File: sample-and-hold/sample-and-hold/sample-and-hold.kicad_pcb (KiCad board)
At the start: 2 copper layers, 36 parts, among them J1 Power Connector, J2 CLOCK_IN, J3 SIGNAL_IN, J4 SIGNAL_IN, Q1 J112, Q2 2N3904, U1 TL072, U2 TL072

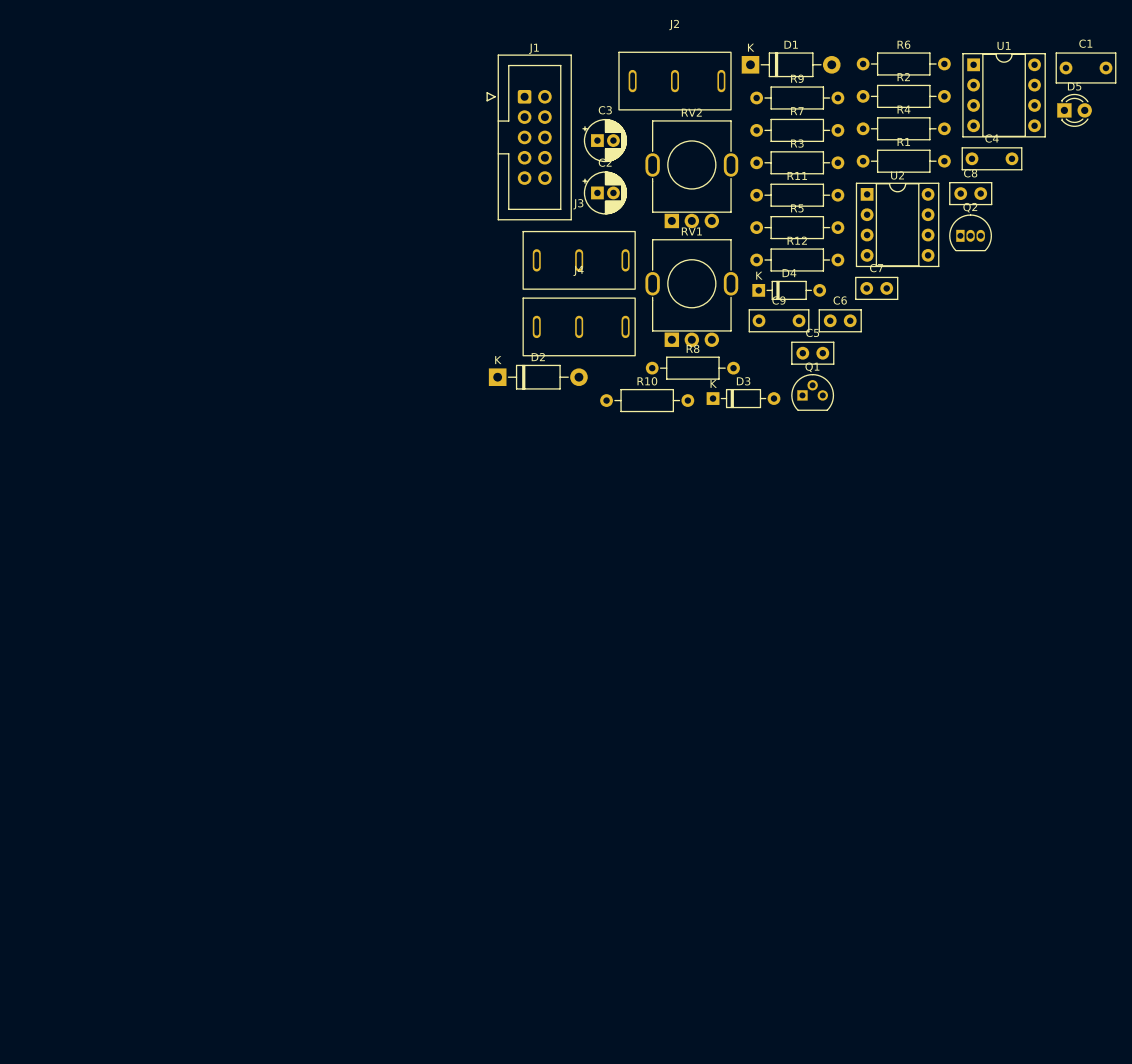
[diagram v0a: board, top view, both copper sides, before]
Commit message: Added REV1 of sample and hold board/panel
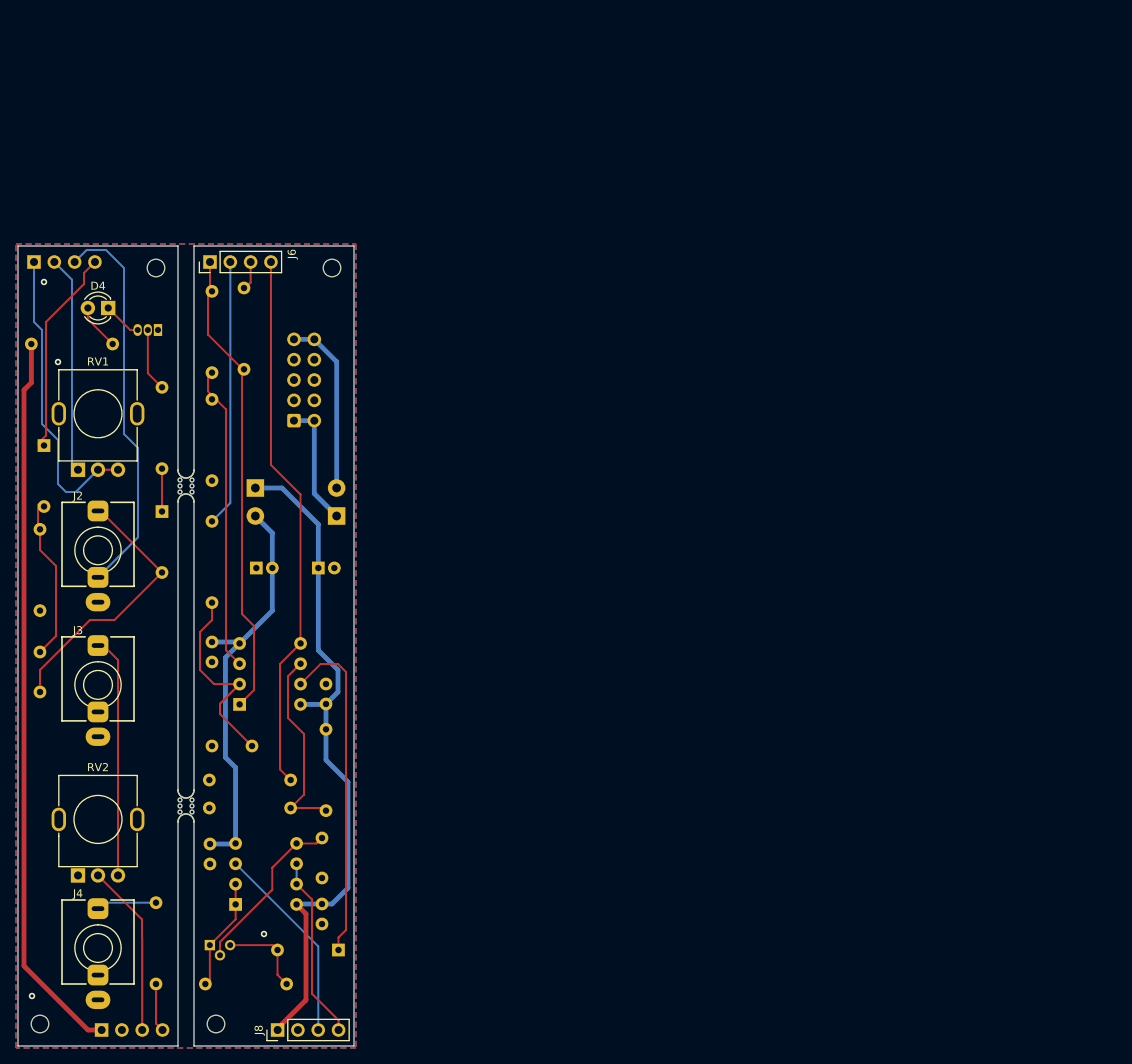
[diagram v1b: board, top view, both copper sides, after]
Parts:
- added D6: 1N4148, Diode_THT:D_DO-35_SOD27_P7.62mm_Horizontal, B.Cu at (180.1, 132.2)
- added H1: MountingHole, MountingHole:MountingHole_2.2mm_M2, F.Cu at (157.2, 47.0)
- added H2: MountingHole, MountingHole:MountingHole_2.2mm_M2, F.Cu at (142.8, 141.5)
- added H3: MountingHole, MountingHole:MountingHole_2.2mm_M2, F.Cu at (179.2, 47.0)
- added H4: MountingHole, MountingHole:MountingHole_2.2mm_M2, F.Cu at (164.8, 141.5)
- added J6: BACK_TOP, Connector_PinHeader_2.54mm:PinHeader_1x04_P2.54mm_Vertical, F.Cu at (164.0, 46.2)
- added J7: FRONT_BOTTOM, Connector_PinHeader_2.54mm:PinHeader_1x04_P2.54mm_Vertical, B.Cu at (150.4, 142.2)
- added J8: BACK_BOTTOM, Connector_PinHeader_2.54mm:PinHeader_1x04_P2.54mm_Vertical, F.Cu at (172.4, 142.2)
- added locked: FRONT_TOP, Connector_PinHeader_2.54mm:PinHeader_1x04_P2.54mm_Vertical, B.Cu at (142.0, 46.2)
- added mouse-bite-2mm-slot: VAL**, Panelization:mouse-bite-2mm-slot, F.Cu at (161.0, 74.2)
- added mouse-bite-2mm-slot: VAL**, Panelization:mouse-bite-2mm-slot, F.Cu at (161.0, 114.2)
- C1: value 1uF -> 10uF; footprint Capacitor_THT:C_Rect_L7.2mm_W3.5mm_P5.00mm_FKS2_FKP2_MKS2_MKP2 -> Capacitor_THT:CP_Radial_D5.0mm_P2.00mm; moved to B.Cu
- C2, C5, C6, C7, C9, D1, D2, D3, J1, R4, R5, U1, U2: moved to B.Cu
- C3: value 10uF -> 1nF; footprint Capacitor_THT:CP_Radial_D5.0mm_P2.00mm -> Capacitor_THT:C_Rect_L7.2mm_W2.5mm_P5.00mm_FKS2_FKP2_MKS2_MKP2; moved to B.Cu
- C4: value 1nF -> 0.1uF; footprint Capacitor_THT:C_Rect_L7.2mm_W2.5mm_P5.00mm_FKS2_FKP2_MKS2_MKP2 -> Capacitor_THT:C_Disc_D5.0mm_W2.5mm_P2.50mm; moved to B.Cu
- C8: value 0.1uF -> 1uF; footprint Capacitor_THT:C_Disc_D5.0mm_W2.5mm_P2.50mm -> Capacitor_THT:C_Rect_L7.2mm_W3.5mm_P5.00mm_FKS2_FKP2_MKS2_MKP2; moved to B.Cu
- D4: value 1N4148 -> LED; footprint Diode_THT:D_DO-35_SOD27_P7.62mm_Horizontal -> LED_THT:LED_D3.0mm
- D5: value LED -> 1N4148; footprint LED_THT:LED_D3.0mm -> Diode_THT:D_DO-35_SOD27_P7.62mm_Horizontal; moved to B.Cu
- J2, J3: footprint Tayda_Jacks:PJ-323M -> AudioJacks:Jack_3.5mm_QingPu_WQP-PJ398SM_Vertical
- J4: value SIGNAL_IN -> SIGNAL_OUT; footprint Tayda_Jacks:PJ-323M -> AudioJacks:Jack_3.5mm_QingPu_WQP-PJ398SM_Vertical
- Q1: value J112 -> 2N3904; footprint Package_TO_SOT_THT:TO-92 -> Package_TO_SOT_THT:TO-92_Inline; moved to B.Cu
- Q2: value 2N3904 -> J112; footprint Package_TO_SOT_THT:TO-92_Inline -> Package_TO_SOT_THT:TO-92; moved to B.Cu
- R1, R3: value 100k -> 1k; moved to B.Cu
- R10: value 51k -> 1M; moved to B.Cu
- R11, R12: value 1k -> 100k; moved to B.Cu
- R2: value 2k -> 51k; moved to B.Cu
- R6: value 100k -> 68k; moved to B.Cu
- R7: value 68k -> 100k; moved to B.Cu
- R8: value 100k -> 2k; moved to B.Cu
- R9: value 1M -> 100k; moved to B.Cu
- moved R1 135.6 mm to (157.2, 136.5), turned to 90 degrees
- moved D5 134.3 mm to (143.2, 69.2), turned to -90 degrees
- moved Q2 129.1 mm to (164.0, 131.6)
- moved U1 121.7 mm to (167.7, 101.5)
- moved R4 119.2 mm to (142.8, 89.8), turned to 90 degrees
- moved U2 118.8 mm to (167.2, 126.5)
- moved R6 117.3 mm to (174.1, 114.5), turned to 180 degrees
- moved C8 116.3 mm to (164.2, 106.8)
- moved C4 112.6 mm to (164.2, 93.8), turned to -90 degrees
- moved C1 112.4 mm to (177.5, 84.5)
- moved RV2 110.5 mm to (150.0, 115.9)
- moved C7 102.7 mm to (178.0, 126.5), turned to -90 degrees
- moved C6 101.4 mm to (164.0, 119.0), turned to -90 degrees
- moved J4 98.2 mm to (150.0, 132.0)
- moved C3 98.0 mm to (142.8, 100.0), turned to 90 degrees
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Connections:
- C1 pad 1: GND -> +12V
- C1 pad 2: Net-(C1-Pad2) -> GND
- C2 pad 1: +12V -> GND
- C2 pad 2: GND -> -12V
- C3 pad 1: GND -> Net-(C3-Pad1)
- C3 pad 2: -12V -> Net-(C3-Pad2)
- C4 pad 1: CLK -> -12V
- C4 pad 2: Net-(C4-Pad2) -> GND
- C5 pad 1: -12V -> +12V
- C6 pad 1: +12V -> -12V
- C7 pad 1: -12V -> +12V
- C8 pad 1: +12V -> GND
- C8 pad 2: GND -> Net-(C8-Pad2)
- D3 pad 2: Net-(C4-Pad2) -> Net-(C3-Pad1)
- D5 pad 1: Net-(D5-Pad1) -> /CLK_FRONT
- D5 pad 2: Net-(D5-Pad2) -> Net-(C3-Pad2)
- J2 pad T: CLK -> Net-(C3-Pad1)
- J2 pad TN: INTERNAL_CLK -> /INT_CLK_FRONT
- Q1 pad 1: Net-(Q1-Pad1) -> GND
- Q1 pad 2: Net-(C9-Pad2) -> Net-(Q1-Pad2)
- Q1 pad 3: Net-(D4-Pad2) -> Net-(D4-Pad1)
- Q2 pad 1: GND -> Net-(Q2-Pad1)
- Q2 pad 2: Net-(Q2-Pad2) -> Net-(C9-Pad2)
- Q2 pad 3: Net-(D5-Pad1) -> Net-(D6-Pad2)
- R1 pad 1: Net-(R1-Pad1) -> /OUT_FRONT
- R1 pad 2: GND -> Net-(J4-PadT)
- R10 pad 1: Net-(Q2-Pad2) -> Net-(D6-Pad2)
- R10 pad 2: CLK -> Net-(Q2-Pad1)
- R11 pad 1: +12V -> /RATE_RTN_BACK
- R11 pad 2: Net-(D5-Pad2) -> Net-(R11-Pad2)
- R12 pad 1: Net-(R12-Pad1) -> /INT_CLK_BACK
- R12 pad 2: Net-(J4-PadT) -> /RATE_RTN_BACK
- R2 pad 1: Net-(R2-Pad1) -> Net-(Q1-Pad2)
- R2 pad 2: Net-(C1-Pad2) -> Net-(D3-Pad1)
- R3 pad 1: Net-(R3-Pad1) -> +12V
- R3 pad 2: Net-(R1-Pad1) -> Net-(D4-Pad2)
- R4 pad 1: INTERNAL_CLK -> GND
- R4 pad 2: Net-(R3-Pad1) -> Net-(C3-Pad2)
- R5 pad 2: Net-(C4-Pad2) -> /CLK_BACK
- R6 pad 1: GND -> Net-(R6-Pad1)
- R6 pad 2: Net-(D3-Pad1) -> GND
- R7 pad 1: Net-(R7-Pad1) -> Net-(R11-Pad2)
- R8 pad 1: +12V -> /RATE_SEND_BACK
- R8 pad 2: Net-(R7-Pad1) -> Net-(C8-Pad2)
- R9 pad 1: Net-(D4-Pad2) -> +12V
- R9 pad 2: Net-(Q1-Pad1) -> Net-(R6-Pad1)
- RV1 pad 1: Net-(R2-Pad1) -> /RATE_SEND_FRONT
- RV1 pad 2: Net-(R3-Pad1) -> /RATE_RTN_FRONT
- RV1 pad 3: Net-(R3-Pad1) -> /RATE_RTN_FRONT
- RV2 pad 1: Net-(J3-PadT) -> GND
- RV2 pad 2: Net-(RV2-Pad2) -> /IN_FRONT
- RV2 pad 3: GND -> Net-(J3-PadT)
- U1 pad 1: Net-(R3-Pad1) -> /RATE_RTN_BACK
- U1 pad 2: Net-(C1-Pad2) -> Net-(C8-Pad2)
- U1 pad 3: Net-(R1-Pad1) -> Net-(R11-Pad2)
- U1 pad 5: Net-(D3-Pad1) -> /CLK_BACK
- U1 pad 6: Net-(R7-Pad1) -> Net-(R6-Pad1)
- U1 pad 7: Net-(D4-Pad1) -> Net-(D6-Pad1)
- U2 pad 1: Net-(Q1-Pad1) -> Net-(Q2-Pad1)
- U2 pad 2: Net-(Q1-Pad1) -> Net-(Q2-Pad1)
- U2 pad 3: Net-(RV2-Pad2) -> /IN_BACK
- U2 pad 6: Net-(R12-Pad1) -> /OUT_BACK
- U2 pad 7: Net-(R12-Pad1) -> /OUT_BACK
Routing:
- net +12V: track 0.00 -> 176.9 mm
- net /CLK_BACK: track 0.00 -> 67.9 mm
- net /RATE_RTN_BACK: track 0.00 -> 58.2 mm
- net -12V: track 0.00 -> 51.2 mm
- net /INT_CLK_FRONT: track 0.00 -> 49.2 mm
- net Net-(D6-Pad1): track 0.00 -> 42.3 mm
- net Net-(R11-Pad2): track 0.00 -> 38.4 mm
- net /RATE_RTN_FRONT: track 0.00 -> 38.1 mm
- net Net-(C3-Pad1): track 0.00 -> 33.9 mm
- net /RATE_SEND_BACK: track 0.00 -> 33.4 mm
- net Net-(J3-PadT): track 0.00 -> 29.5 mm
- net /RATE_SEND_FRONT: track 0.00 -> 26.1 mm
- net /CLK_FRONT: track 0.00 -> 25.6 mm
- net Net-(C8-Pad2): track 0.00 -> 25.1 mm
- net /IN_BACK: track 0.00 -> 25.1 mm
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- added copper zone on B.Cu, net GND
- added copper zone on F.Cu, net GND
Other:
- board outline added: 42 x 100 mm

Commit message: Added revision text to sample and hold board/panel
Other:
- board text added: "Northridge Devices - Sept 2022"
- board text added: "S&H Board A - REV1"
- board text added: "S&H Board B - REV1"
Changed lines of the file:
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@@
     (fp_arc (start -2 -1) (mid -1 0) (end -2 1) (layer "F.SilkS") (width 0.1))
     (fp_arc (start 2 1) (mid 1 0) (end 2 -1) (layer "F.SilkS") (width 0.1))
+    (fp_circle (center -2 0) (end -2 -0.06) (layer "Dwgs.User") (width 0.05) (fill none))
     (fp_circle (center 2 0) (end 2.06 0) (layer "Dwgs.User") (width 0.05) (fill none))
-    (fp_circle (center -2 0) (end -2 -0.06) (layer "Dwgs.User") (width 0.05) (fill none))
     (fp_line (start -2 0) (end -2 0) (layer "Eco1.User") (width 2))
     (fp_line (start 2 0) (end 2 0) (layer "Eco1.User") (width 2))
+    (pad "" np_thru_hole circle locked (at 0 -0.75 90) (size 0.5 0.5) (drill 0.5) (layers *.Cu *.Mask))
+    (pad "" np_thru_hole circle locked (at 0.75 -0.75 90) (size 0.5 0.5) (drill 0.5) (layers *.Cu *.Mask))
     (pad "" np_thru_hole circle locked (at 0.75 0.75 90) (size 0.5 0.5) (drill 0.5) (layers *.Cu *.Mask))
+    (pad "" np_thru_hole circle locked (at 0 0.75 90) (size 0.5 0.5) (drill 0.5) (layers *.Cu *.Mask))
+    (pad "" np_thru_hole circle locked (at -0.75 -0.75 90) (size 0.5 0.5) (drill 0.5) (layers *.Cu *.Mask))
     (pad "" np_thru_hole circle locked (at -0.75 0.75 90) (size 0.5 0.5) (drill 0.5) (layers *.Cu *.Mask))
-    (pad "" np_thru_hole circle locked (at -0.75 -0.75 90) (size 0.5 0.5) (drill 0.5) (layers *.Cu *.Mask))
-    (pad "" np_thru_hole circle locked (at 0 0.75 90) (size 0.5 0.5) (drill 0.5) (layers *.Cu *.Mask))
-    (pad "" np_thru_hole circle locked (at 0.75 -0.75 90) (size 0.5 0.5) (drill 0.5) (layers *.Cu *.Mask))
-    (pad "" np_thru_hole circle locked (at 0 -0.75 90) (size 0.5 0.5) (drill 0.5) (layers *.Cu *.Mask))
   )
   (footprint "MountingHole:MountingHole_2.2mm_M2" locked (layer "F.Cu")
@@
   (gr_arc (start 162 112.25) (mid 161 113.25) (end 160 112.25) (layer "Edge.Cuts") (width 0.1))
   (gr_line locked (start 182 44.25) (end 182 144.25) (layer "Edge.Cuts") (width 0.1))
+  (gr_text "S&H Board A - REV1" (at 141.5 128.75 90) (layer "F.SilkS")
+    (effects (font (size 1 1) (thickness 0.15)))
+  )
+  (gr_text "S&H Board B - REV1" (at 180.75 110 90) (layer "F.SilkS")
+    (effects (font (size 1 1) (thickness 0.15)))
+  )
+  (gr_text "Northridge Devices - Sept 2022" (at 157.75 101.75 90) (layer "F.SilkS")
+    (effects (font (size 1 1) (thickness 0.15)))
+  )
   (dimension (type aligned) (layer "Dwgs.User")
     (pts (xy 160 44.25) (xy 140 44.25))
